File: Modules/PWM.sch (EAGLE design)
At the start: 32 parts, among them J3 2X6 FEMALE

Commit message: Added frame
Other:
- note added: "(c) DART 2018 The PWM Module allows us to have 16 PWM channels per module on the main board. Being a module, it is fully replacable or upgradable if the need arises."
- note added: "A"
- note added: "PoolTable PWM Module"
- moved on the sheet: C1, D1, J1, J2, J3, R1, R2, R24, R25, R26, R3, R4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

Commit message: Added Connectors and Molex
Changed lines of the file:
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@@
 <?xml version="1.0" encoding="utf-8"?>
 <!DOCTYPE eagle SYSTEM "eagle.dtd">
-<eagle version="9.2.2">
+<eagle version="9.3.0">
 <drawing>
 <settings>
@@
 <wire x1="27.94" y1="152.4" x2="27.94" y2="154.94" width="0.1524" layer="91"/>
 <wire x1="27.94" y1="154.94" x2="27.94" y2="157.48" width="0.1524" layer="91"/>
-<wire x1="27.94" y1="157.48" x2="27.94" y2="160.02" width="0.1524" layer="91"/>
-<wire x1="27.94" y1="160.02" x2="27.94" y2="162.56" width="0.1524" layer="91"/>
-<wire x1="27.94" y1="162.56" x2="27.94" y2="167.64" width="0.1524" layer="91"/>
+<wire x1="27.94" y1="157.48" x2="27.94" y2="167.64" width="0.1524" layer="91"/>
 <wire x1="33.02" y1="147.32" x2="27.94" y2="147.32" width="0.1524" layer="91"/>
 <junction x="27.94" y="147.32"/>
@@
 <wire x1="33.02" y1="157.48" x2="27.94" y2="157.48" width="0.1524" layer="91"/>
 <junction x="27.94" y="157.48"/>
-<wire x1="33.02" y1="160.02" x2="27.94" y2="160.02" width="0.1524" layer="91"/>
-<junction x="27.94" y="160.02"/>
-<wire x1="33.02" y1="162.56" x2="27.94" y2="162.56" width="0.1524" layer="91"/>
-<junction x="27.94" y="162.56"/>
 <pinref part="J3" gate="G$1" pin="9"/>
 <pinref part="J3" gate="G$1" pin="7"/>

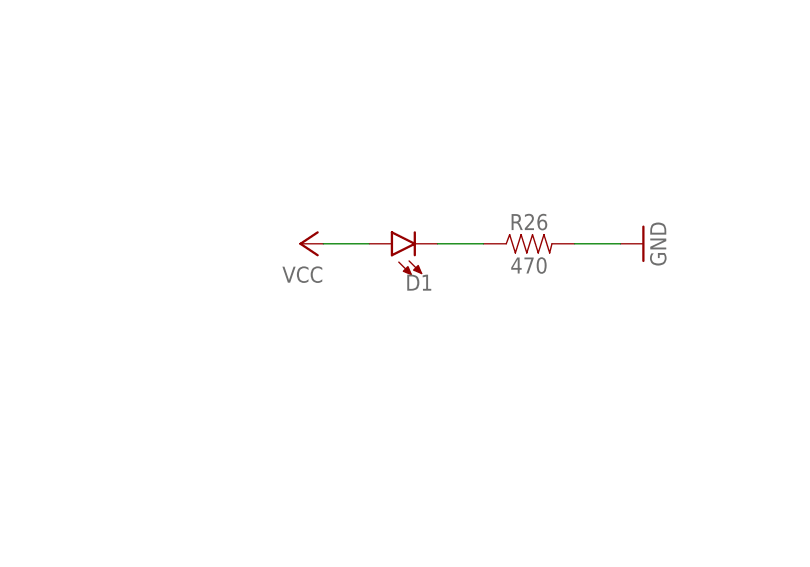
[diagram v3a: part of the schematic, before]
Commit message: Sending PWM Module to Fab
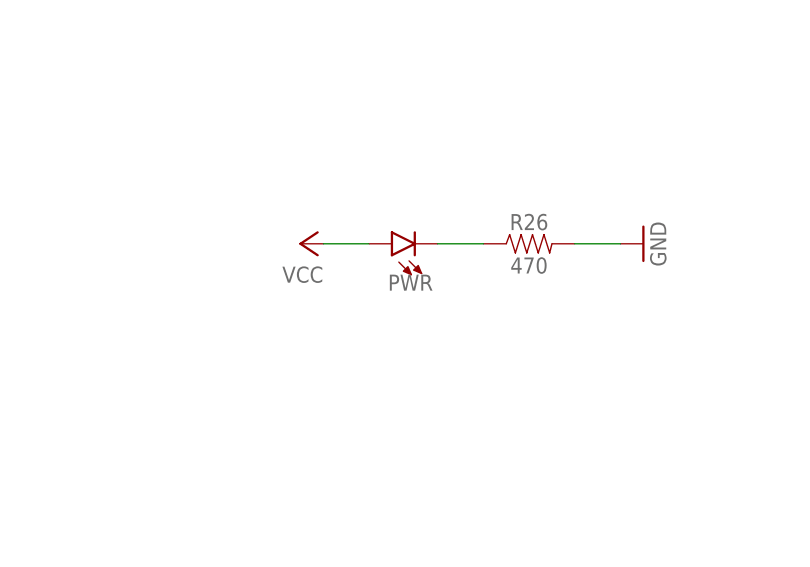
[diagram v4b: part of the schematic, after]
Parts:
- renumbered D1 to PWR
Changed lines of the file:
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@@
 <?xml version="1.0" encoding="utf-8"?>
 <!DOCTYPE eagle SYSTEM "eagle.dtd">
-<eagle version="9.3.0">
+<eagle version="9.3.1">
 <drawing>
 <settings>
@@
 <part name="P+4" library="supply1" library_urn="urn:adsk.eagle:library:371" deviceset="VCC" device=""/>
 <part name="P+5" library="supply1" library_urn="urn:adsk.eagle:library:371" deviceset="VCC" device=""/>
-<part name="D1" library="SparkFun-LED" deviceset="LED" device="0603"/>
+<part name="PWR" library="SparkFun-LED" deviceset="LED" device="0603"/>
 <part name="R26" library="SparkFun-Resistors" deviceset="470OHM" device="-0603-1/10W-1%" value="470"/>
 <part name="GND6" library="supply1" library_urn="urn:adsk.eagle:library:371" deviceset="GND" device=""/>
@@
 <instance part="P+4" gate="VCC" x="198.12" y="58.42" smashed="yes" rot="R90"/>
 <instance part="P+5" gate="VCC" x="238.76" y="63.5" smashed="yes" rot="R270"/>
-<instance part="D1" gate="D1" x="187.96" y="144.78" smashed="yes" rot="R90">
+<instance part="PWR" gate="D1" x="187.96" y="144.78" smashed="yes" rot="R90">
 <attribute name="NAME" x="192.532" y="141.351" size="1.778" layer="95" font="vector" rot="R180"/>
 <attribute name="VALUE" x="192.532" y="146.685" size="1.778" layer="96" font="vector" rot="R180" align="top-left"/>
@@
 <segment>
 <pinref part="P+6" gate="VCC" pin="VCC"/>
-<pinref part="D1" gate="D1" pin="A"/>
+<pinref part="PWR" gate="D1" pin="A"/>
 <wire x1="180.34" y1="144.78" x2="185.42" y2="144.78" width="0.1524" layer="91"/>
 </segment>
@@
 <net name="N$18" class="0">
 <segment>
-<pinref part="D1" gate="D1" pin="C"/>
+<pinref part="PWR" gate="D1" pin="C"/>
 <pinref part="R26" gate="G$1" pin="1"/>
 <wire x1="193.04" y1="144.78" x2="198.12" y2="144.78" width="0.1524" layer="91"/>

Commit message: Auto stash before merge of "master" and "origin/master"
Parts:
- R26: value 470 -> 100R
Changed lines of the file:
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@@
 <part name="P+5" library="supply1" library_urn="urn:adsk.eagle:library:371" deviceset="VCC" device=""/>
 <part name="PWR" library="SparkFun-LED" deviceset="LED" device="0603"/>
-<part name="R26" library="SparkFun-Resistors" deviceset="470OHM" device="-0603-1/10W-1%" value="470"/>
+<part name="R26" library="SparkFun-Resistors" deviceset="470OHM" device="-0603-1/10W-1%" value="100R"/>
 <part name="GND6" library="supply1" library_urn="urn:adsk.eagle:library:371" deviceset="GND" device=""/>
 <part name="P+6" library="supply1" library_urn="urn:adsk.eagle:library:371" deviceset="VCC" device=""/>
